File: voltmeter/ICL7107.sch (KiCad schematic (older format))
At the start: 38 parts, among them J1 +9...12V DC, J2 DP conn., J3 meas. conn, M1 M2.2, M2 M2.2, M3 M2.2, M4 M2.2, U1 LM285Z-1.2, U2 ICL7107, U3 L7805

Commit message: updated file
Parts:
- G1: footprint logo:logo-cc-by-sa-1 -> logo-sq7eqe:cc-by-sa
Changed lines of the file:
@@
 F 0 "G1" H 4850 7291 60  0001 C CNN
 F 1 "CC-BY-SA" H 4850 7509 60  0001 C CNN
-F 2 "logo:logo-cc-by-sa-1" H 4850 7400 50  0001 C CNN
+F 2 "logo-sq7eqe:cc-by-sa" H 4850 7400 50  0001 C CNN
 F 3 "" H 4850 7400 50  0001 C CNN
 	1    4850 7400

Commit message: update file
I make mistake in schematics library & footprint library
now devices are correct, I divided 7 segment display at
two separate CA & CC

bye!
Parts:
- removed D1: LED-Display_x4, LED-display_x4:LED-Display_x4_package, symbol LED_Display:LED-Display_x4
- added D1: LED-Display_x4_CA, LED-display_x4:LED-Display_x4_package, symbol LED_Display:LED-Display_x4_CA
- renumbered D3 to D2, D4 to D3, D5 to D4, D6 to D5, D7 to D6
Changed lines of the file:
@@
 $EndComp
 $Comp
-L Diode:1N4001 D3
+L Diode:1N4001 D2
 U 1 1 5ECC12B1
 P 7500 1500
-F 0 "D3" H 7500 1283 50  0000 C CNN
+F 0 "D2" H 7500 1283 50  0000 C CNN
 F 1 "1N4001" H 7500 1374 50  0000 C CNN
 F 2 "Diode_THT:D_DO-41_SOD81_P10.16mm_Horizontal" H 7500 1325 50  0001 C CNN
@@
 	6100 3400 6250 3400
 $Comp
-L Diode:1N4001 D7
+L Diode:1N4001 D6
 U 1 1 5ED0FC3E
 P 7500 4350
-F 0 "D7" V 7546 4270 50  0000 R CNN
+F 0 "D6" V 7546 4270 50  0000 R CNN
 F 1 "1N4001" V 7455 4270 50  0000 R CNN
 F 2 "Diode_THT:D_DO-41_SOD81_P10.16mm_Horizontal" H 7500 4175 50  0001 C CNN
@@
 $EndComp
 $Comp
-L Diode:1N4001 D6
+L Diode:1N4001 D5
 U 1 1 5ED10897
 P 7500 3950
-F 0 "D6" V 7546 3870 50  0000 R CNN
+F 0 "D5" V 7546 3870 50  0000 R CNN
 F 1 "1N4001" V 7455 3870 50  0000 R CNN
 F 2 "Diode_THT:D_DO-41_SOD81_P10.16mm_Horizontal" H 7500 3775 50  0001 C CNN
@@
 $EndComp
 $Comp
-L Diode:1N4001 D5
+L Diode:1N4001 D4
 U 1 1 5ED10E1C
 P 7500 3550
-F 0 "D5" V 7546 3470 50  0000 R CNN
+F 0 "D4" V 7546 3470 50  0000 R CNN
 F 1 "1N4001" V 7455 3470 50  0000 R CNN
 F 2 "Diode_THT:D_DO-41_SOD81_P10.16mm_Horizontal" H 7500 3375 50  0001 C CNN
@@
 $EndComp
 $Comp
-L Diode:1N4001 D4
+L Diode:1N4001 D3
 U 1 1 5ED1133D
 P 7500 3150
-F 0 "D4" V 7546 3070 50  0000 R CNN
+F 0 "D3" V 7546 3070 50  0000 R CNN
 F 1 "1N4001" V 7455 3070 50  0000 R CNN
 F 2 "Diode_THT:D_DO-41_SOD81_P10.16mm_Horizontal" H 7500 2975 50  0001 C CNN
@@
 	2550 3250 3000 3250
 $Comp
-L LED_Display:LED-Display_x4 D1
-U 1 1 5ECF9A78
-P 5450 2200
-F 0 "D1" V 4525 2475 50  0000 C CNN
-F 1 "LED-Display_x4" V 4616 2475 50  0000 C CNN
-F 2 "LED-display_x4:LED-Display_x4_package" H 5450 2450 50  0001 C CNN
-F 3 "" H 5450 2200 50  0001 C CNN
-	1    5450 2200
-	0    1    1    0
-$EndComp
-$Comp
-L LED_Display:LED-Display_x4 D1
-U 2 1 5ECFC1DC
-P 5450 3800
-F 0 "D1" V 6250 4050 50  0000 C CNN
-F 1 "LED-Display_x4" V 6350 4050 50  0000 C CNN
-F 2 "LED-display_x4:LED-Display_x4_package" H 5450 4050 50  0001 C CNN
-F 3 "" H 5450 3800 50  0001 C CNN
-	2    5450 3800
-	0    1    1    0
-$EndComp
-$Comp
 L Graphic:Logo_Open_Hardware_Large LOGO1
 U 1 1 5ED11310
@@
 F1 "file5ECBC5A0.sch" 50
 $EndSheet
+$Comp
+L LED_Display:LED-Display_x4_CA D1
+U 1 1 5EFBBD4C
+P 5450 2200
+F 0 "D1" V 4525 2475 50  0000 C CNN
+F 1 "LED-Display_x4_CA" V 4616 2475 50  0000 C CNN
+F 2 "LED-display_x4:LED-Display_x4_package" H 5450 2450 50  0001 C CNN
+F 3 "" H 5450 2200 50  0001 C CNN
+	1    5450 2200
+	0    1    1    0
+$EndComp
+$Comp
+L LED_Display:LED-Display_x4_CA D1
+U 2 1 5EFBDD2C
+P 5450 3800
+F 0 "D1" V 6250 4050 50  0000 C CNN
+F 1 "LED-Display_x4_CA" V 6350 4100 50  0000 C CNN
+F 2 "LED-display_x4:LED-Display_x4_package" H 5450 4050 50  0001 C CNN
+F 3 "" H 5450 3800 50  0001 C CNN
+	2    5450 3800
+	0    1    1    0
+$EndComp
 $EndSCHEMATC

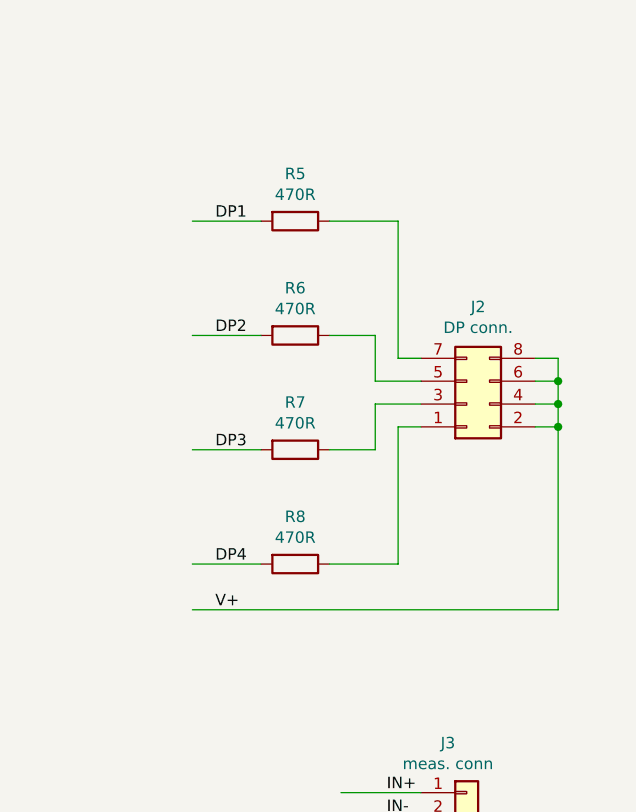
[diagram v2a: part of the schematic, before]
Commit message: update
Zmodyfikowałem schemat i tym samym projekt płytki drukowanej
usunąłem zbędne rezystory i poprawnie połączyłem dp wyświetlaczy
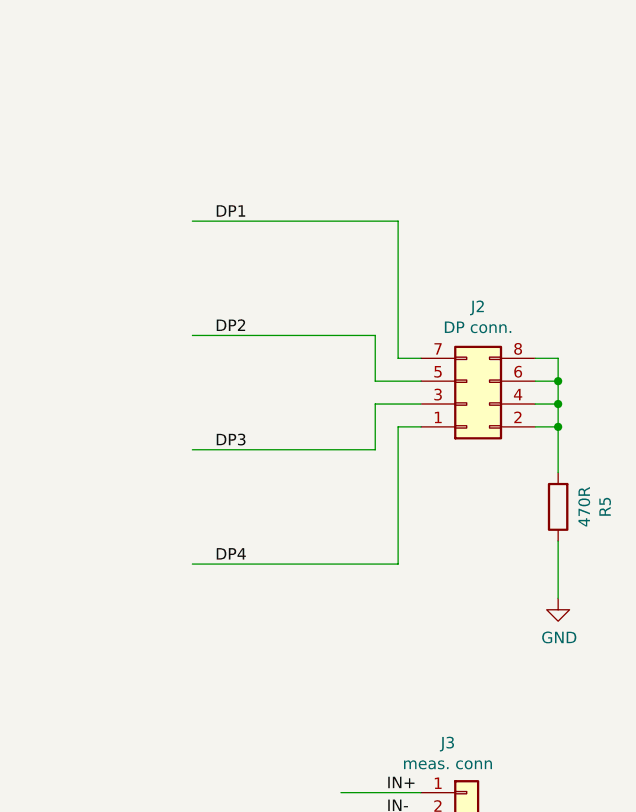
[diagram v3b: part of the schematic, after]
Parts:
- removed R5, R6, R7: 470R, Resistor_THT:R_Axial_DIN0204_L3.6mm_D1.6mm_P2.54mm_Vertical, symbol Device:R
- renumbered R8 to R5
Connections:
- wire segments 143 -> 139
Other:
- moved on the sheet: R5
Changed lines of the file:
@@
 $Comp
 L Device:R R5
-U 1 1 5ECE8796
-P 9150 3000
-F 0 "R5" V 8943 3000 50  0000 C CNN
-F 1 "470R" V 9034 3000 50  0000 C CNN
-F 2 "Resistor_THT:R_Axial_DIN0204_L3.6mm_D1.6mm_P2.54mm_Vertical" V 9080 3000 50  0001 C CNN
-F 3 "~" H 9150 3000 50  0001 C CNN
-	1    9150 3000
-	0    1    1    0
-$EndComp
-$Comp
-L Device:R R6
-U 1 1 5ECE8ED1
-P 9150 3500
-F 0 "R6" V 8943 3500 50  0000 C CNN
-F 1 "470R" V 9034 3500 50  0000 C CNN
-F 2 "Resistor_THT:R_Axial_DIN0204_L3.6mm_D1.6mm_P2.54mm_Vertical" V 9080 3500 50  0001 C CNN
-F 3 "~" H 9150 3500 50  0001 C CNN
-	1    9150 3500
-	0    1    1    0
-$EndComp
-$Comp
-L Device:R R7
-U 1 1 5ECE934A
-P 9150 4000
-F 0 "R7" V 8943 4000 50  0000 C CNN
-F 1 "470R" V 9034 4000 50  0000 C CNN
-F 2 "Resistor_THT:R_Axial_DIN0204_L3.6mm_D1.6mm_P2.54mm_Vertical" V 9080 4000 50  0001 C CNN
-F 3 "~" H 9150 4000 50  0001 C CNN
-	1    9150 4000
-	0    1    1    0
-$EndComp
-$Comp
-L Device:R R8
 U 1 1 5ECE9732
-P 9150 4500
-F 0 "R8" V 8943 4500 50  0000 C CNN
-F 1 "470R" V 9034 4500 50  0000 C CNN
-F 2 "Resistor_THT:R_Axial_DIN0204_L3.6mm_D1.6mm_P2.54mm_Vertical" V 9080 4500 50  0001 C CNN
-F 3 "~" H 9150 4500 50  0001 C CNN
-	1    9150 4500
-	0    1    1    0
+P 10300 4250
+F 0 "R5" V 10093 4250 50  0000 C CNN
+F 1 "470R" V 10184 4250 50  0000 C CNN
+F 2 "Resistor_THT:R_Axial_DIN0204_L3.6mm_D1.6mm_P2.54mm_Vertical" V 10230 4250 50  0001 C CNN
+F 3 "~" H 10300 4250 50  0001 C CNN
+	1    10300 4250
+	-1   0    0    1
 $EndComp
 Wire Wire Line
@@
 DP4
 Wire Wire Line
-	9300 3500 9500 3500
-Wire Wire Line
 	9500 3500 9500 3700
 Wire Wire Line
 	9500 3700 9700 3700
 Wire Wire Line
-	9300 4000 9500 4000
-Wire Wire Line
 	9500 4000 9500 3800
 Wire Wire Line
 	9500 3800 9700 3800
 Wire Wire Line
-	9300 4500 9600 4500
-Wire Wire Line
 	9600 4500 9600 3900
 Wire Wire Line
 	9600 3900 9700 3900
 Wire Wire Line
-	9300 3000 9600 3000
-Wire Wire Line
 	9600 3000 9600 3600
 Wire Wire Line
 	9600 3600 9700 3600
-Wire Wire Line
-	9000 3000 8700 3000
-Wire Wire Line
-	9000 3500 8700 3500
-Wire Wire Line
-	9000 4000 8700 4000
-Wire Wire Line
-	9000 4500 8700 4500
-Text Label 8800 4700 0    50   ~ 0
-V+
 Text Label 8800 3000 0    50   ~ 0
 DP1
@@
 	10300 3600 10300 3700
 Wire Wire Line
-	8700 4700 10300 4700
-Wire Wire Line
 	10200 3900 10300 3900
-Connection ~ 10300 3900
-Wire Wire Line
-	10300 3900 10300 4700
 Wire Wire Line
 	10200 3800 10300 3800
@@
 	0    1    1    0
 $EndComp
+$Comp
+L power:GND #PWR03
+U 1 1 5F01191C
+P 10300 4650
+F 0 "#PWR03" H 10300 4400 50  0001 C CNN
+F 1 "GND" H 10305 4477 50  0000 C CNN
+F 2 "" H 10300 4650 50  0001 C CNN
+F 3 "" H 10300 4650 50  0001 C CNN
+	1    10300 4650
+	1    0    0    -1
+$EndComp
+Wire Wire Line
+	8700 3000 9600 3000
+Wire Wire Line
+	8700 3500 9500 3500
+Wire Wire Line
+	8700 4000 9500 4000
+Wire Wire Line
+	8700 4500 9600 4500
+Wire Wire Line
+	10300 3900 10300 4100
+Connection ~ 10300 3900
+Wire Wire Line
+	10300 4400 10300 4650
 $EndSCHEMATC

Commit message: update file
poprawiłem schemat i ponownie wygenerowałem pliki Gerber

I corrected the diagram and re-generated the Gerber files
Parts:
- added D1, D2: 1N4148, Diode_THT:D_DO-35_SOD27_P7.62mm_Horizontal, symbol Diode:1N4148
- renumbered D1 to D3, D2 to D4, D3 to D5, D4 to D6, D5 to D7, D6 to D8, R2 to R1, R1 to R2
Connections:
- net labels removed: IN-
- wire segments 139 -> 145
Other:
- moved on the sheet: R1
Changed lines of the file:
@@
 Sheet 1 2
 Title "Digital Voltmeter Module ICL7107"
-Date "2020-05-28"
-Rev "1.0"
+Date "2020-07-05"
+Rev "1.5"
 Comp "MSc. Paweł Sobótka"
 Comment1 "CC-BY-SA 4.0"
@@
 	3000 4100 3000 3950
 $Comp
-L Device:R R2
+L Device:R R1
 U 1 1 5ECC9A9E
-P 3050 2700
-F 0 "R2" V 2843 2700 50  0000 C CNN
-F 1 "1M" V 2934 2700 50  0000 C CNN
-F 2 "Resistor_THT:R_Axial_DIN0204_L3.6mm_D1.6mm_P7.62mm_Horizontal" V 2980 2700 50  0001 C CNN
-F 3 "~" H 3050 2700 50  0001 C CNN
-	1    3050 2700
+P 1650 2700
+F 0 "R1" V 1443 2700 50  0000 C CNN
+F 1 "1M" V 1534 2700 50  0000 C CNN
+F 2 "Resistor_THT:R_Axial_DIN0204_L3.6mm_D1.6mm_P7.62mm_Horizontal" V 1580 2700 50  0001 C CNN
+F 3 "~" H 1650 2700 50  0001 C CNN
+	1    1650 2700
 	0    1    1    0
 $EndComp
@@
 Connection ~ 3550 2700
 Wire Wire Line
-	3550 2700 3200 2700
-Wire Wire Line
 	3900 2850 3800 2850
 Wire Wire Line
@@
 	3550 3000 3550 2950
 Connection ~ 3800 3000
-Connection ~ 3550 3000
-Text Label 2550 2700 0    50   ~ 0
-IN+
-Text Label 2550 3000 0    50   ~ 0
-IN-
-$Comp
-L Device:R R1
+$Comp
+L Device:R R2
 U 1 1 5ECD43B4
 P 2600 3700
-F 0 "R1" V 2393 3700 50  0000 C CNN
+F 0 "R2" V 2393 3700 50  0000 C CNN
 F 1 "6k8" V 2484 3700 50  0000 C CNN
 F 2 "Resistor_THT:R_Axial_DIN0204_L3.6mm_D1.6mm_P7.62mm_Horizontal" V 2530 3700 50  0001 C CNN
@@
 $EndComp
 $Comp
-L Diode:1N4001 D2
+L Diode:1N4001 D4
 U 1 1 5ECC12B1
 P 7500 1500
-F 0 "D2" H 7500 1283 50  0000 C CNN
+F 0 "D4" H 7500 1283 50  0000 C CNN
 F 1 "1N4001" H 7500 1374 50  0000 C CNN
 F 2 "Diode_THT:D_DO-41_SOD81_P10.16mm_Horizontal" H 7500 1325 50  0001 C CNN
@@
 	9500 1500 10050 1500
 $Comp
-L power:GND #PWR02
+L power:GND #PWR03
 U 1 1 5ECC92E2
 P 7150 2000
-F 0 "#PWR02" H 7150 1750 50  0001 C CNN
+F 0 "#PWR03" H 7150 1750 50  0001 C CNN
 F 1 "GND" H 7155 1827 50  0000 C CNN
 F 2 "" H 7150 2000 50  0001 C CNN
@@
 Connection ~ 7150 2000
 $Comp
-L power:GND #PWR01
+L power:GND #PWR02
 U 1 1 5ECD4E53
 P 4450 4850
-F 0 "#PWR01" H 4450 4600 50  0001 C CNN
+F 0 "#PWR02" H 4450 4600 50  0001 C CNN
 F 1 "GND" H 4455 4677 50  0000 C CNN
 F 2 "" H 4450 4850 50  0001 C CNN
@@
 	6100 3400 6250 3400
 $Comp
-L Diode:1N4001 D6
+L Diode:1N4001 D8
 U 1 1 5ED0FC3E
 P 7500 4350
-F 0 "D6" V 7546 4270 50  0000 R CNN
+F 0 "D8" V 7546 4270 50  0000 R CNN
 F 1 "1N4001" V 7455 4270 50  0000 R CNN
 F 2 "Diode_THT:D_DO-41_SOD81_P10.16mm_Horizontal" H 7500 4175 50  0001 C CNN
@@
 $EndComp
 $Comp
-L Diode:1N4001 D5
+L Diode:1N4001 D7
 U 1 1 5ED10897
 P 7500 3950
-F 0 "D5" V 7546 3870 50  0000 R CNN
+F 0 "D7" V 7546 3870 50  0000 R CNN
 F 1 "1N4001" V 7455 3870 50  0000 R CNN
 F 2 "Diode_THT:D_DO-41_SOD81_P10.16mm_Horizontal" H 7500 3775 50  0001 C CNN
@@
 $EndComp
 $Comp
-L Diode:1N4001 D4
+L Diode:1N4001 D6
 U 1 1 5ED10E1C
 P 7500 3550
-F 0 "D4" V 7546 3470 50  0000 R CNN
+F 0 "D6" V 7546 3470 50  0000 R CNN
 F 1 "1N4001" V 7455 3470 50  0000 R CNN
 F 2 "Diode_THT:D_DO-41_SOD81_P10.16mm_Horizontal" H 7500 3375 50  0001 C CNN
@@
 $EndComp
 $Comp
-L Diode:1N4001 D3
+L Diode:1N4001 D5
 U 1 1 5ED1133D
 P 7500 3150
-F 0 "D3" V 7546 3070 50  0000 R CNN
+F 0 "D5" V 7546 3070 50  0000 R CNN
 F 1 "1N4001" V 7455 3070 50  0000 R CNN
 F 2 "Diode_THT:D_DO-41_SOD81_P10.16mm_Horizontal" H 7500 2975 50  0001 C CNN
@@
 	1    0    0    -1
 $EndComp
-Wire Wire Line
-	2300 2700 2900 2700
-Wire Wire Line
-	2300 3000 3550 3000
 $Comp
 L logo-sq7eqe:CC-BY-SA G1
@@
 Wire Wire Line
 	9700 5500 9350 5500
-Wire Wire Line
-	9700 5600 9350 5600
 Text Label 9550 5500 0    50   ~ 0
 IN+
-Text Label 9550 5600 0    50   ~ 0
-IN-
 $Comp
 L Connector_Generic:Conn_02x04_Odd_Even J2
@@
 $EndSheet
 $Comp
-L LED_Display:LED-Display_x4_CA D1
+L LED_Display:LED-Display_x4_CA D3
 U 1 1 5EFBBD4C
 P 5450 2200
-F 0 "D1" V 4525 2475 50  0000 C CNN
+F 0 "D3" V 4525 2475 50  0000 C CNN
 F 1 "LED-Display_x4_CA" V 4616 2475 50  0000 C CNN
 F 2 "LED-display_x4:LED-Display_x4_package" H 5450 2450 50  0001 C CNN
@@
 $EndComp
 $Comp
-L LED_Display:LED-Display_x4_CA D1
+L LED_Display:LED-Display_x4_CA D3
 U 2 1 5EFBDD2C
 P 5450 3800
-F 0 "D1" V 6250 4050 50  0000 C CNN
+F 0 "D3" V 6250 4050 50  0000 C CNN
 F 1 "LED-Display_x4_CA" V 6350 4100 50  0000 C CNN
 F 2 "LED-display_x4:LED-Display_x4_package" H 5450 4050 50  0001 C CNN
@@
 $EndComp
 $Comp
-L power:GND #PWR03
+L power:GND #PWR05
 U 1 1 5F01191C
 P 10300 4650
-F 0 "#PWR03" H 10300 4400 50  0001 C CNN
+F 0 "#PWR05" H 10300 4400 50  0001 C CNN
 F 1 "GND" H 10305 4477 50  0000 C CNN
 F 2 "" H 10300 4650 50  0001 C CNN
@@
 Wire Wire Line
 	10300 4400 10300 4650
+$Comp
+L Diode:1N4148 D1
+U 1 1 5F024FA0
+P 2000 2450
+F 0 "D1" V 1954 2530 50  0000 L CNN
+F 1 "1N4148" V 2045 2530 50  0000 L CNN
+F 2 "Diode_THT:D_DO-35_SOD27_P7.62mm_Horizontal" H 2000 2275 50  0001 C CNN
+F 3 "https://assets.nexperia.com/documents/data-sheet/1N4148_1N4448.pdf" H 2000 2450 50  0001 C CNN
+	1    2000 2450
+	0    1    1    0
+$EndComp
+$Comp
+L Diode:1N4148 D2
+U 1 1 5F0256FE
+P 2000 2950
+F 0 "D2" V 1954 3030 50  0000 L CNN
+F 1 "1N4148" V 2045 3030 50  0000 L CNN
+F 2 "Diode_THT:D_DO-35_SOD27_P7.62mm_Horizontal" H 2000 2775 50  0001 C CNN
+F 3 "https://assets.nexperia.com/documents/data-sheet/1N4148_1N4448.pdf" H 2000 2950 50  0001 C CNN
+	1    2000 2950
+	0    1    1    0
+$EndComp
+Wire Wire Line
+	1800 2700 2000 2700
+Wire Wire Line
+	2000 2600 2000 2700
+Connection ~ 2000 2700
+Wire Wire Line
+	2000 2700 3550 2700
+Wire Wire Line
+	2000 2700 2000 2800
+Wire Wire Line
+	2000 2300 2000 2000
+Wire Wire Line
+	2000 3100 2000 3400
+$Comp
+L power:GND #PWR01
+U 1 1 5F042084
+P 3100 3000
+F 0 "#PWR01" H 3100 2750 50  0001 C CNN
+F 1 "GND" H 3105 2827 50  0000 C CNN
+F 2 "" H 3100 3000 50  0001 C CNN
+F 3 "" H 3100 3000 50  0001 C CNN
+	1    3100 3000
+	0    1    1    0
+$EndComp
+Wire Wire Line
+	3550 3000 3100 3000
+Connection ~ 3550 3000
+Wire Wire Line
+	1500 2700 1150 2700
+Text Label 1250 2700 0    50   ~ 0
+IN+
+$Comp
+L power:GND #PWR04
+U 1 1 5F04FE13
+P 9550 5650
+F 0 "#PWR04" H 9550 5400 50  0001 C CNN
+F 1 "GND" H 9555 5477 50  0000 C CNN
+F 2 "" H 9550 5650 50  0001 C CNN
+F 3 "" H 9550 5650 50  0001 C CNN
+	1    9550 5650
+	1    0    0    -1
+$EndComp
+Wire Wire Line
+	9700 5600 9550 5600
+Wire Wire Line
+	9550 5600 9550 5650
+Text Label 2000 2200 0    50   ~ 0
+V+
+Text Label 2000 3250 0    50   ~ 0
+V-
 $EndSCHEMATC
